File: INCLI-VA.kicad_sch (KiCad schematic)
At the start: 0 parts

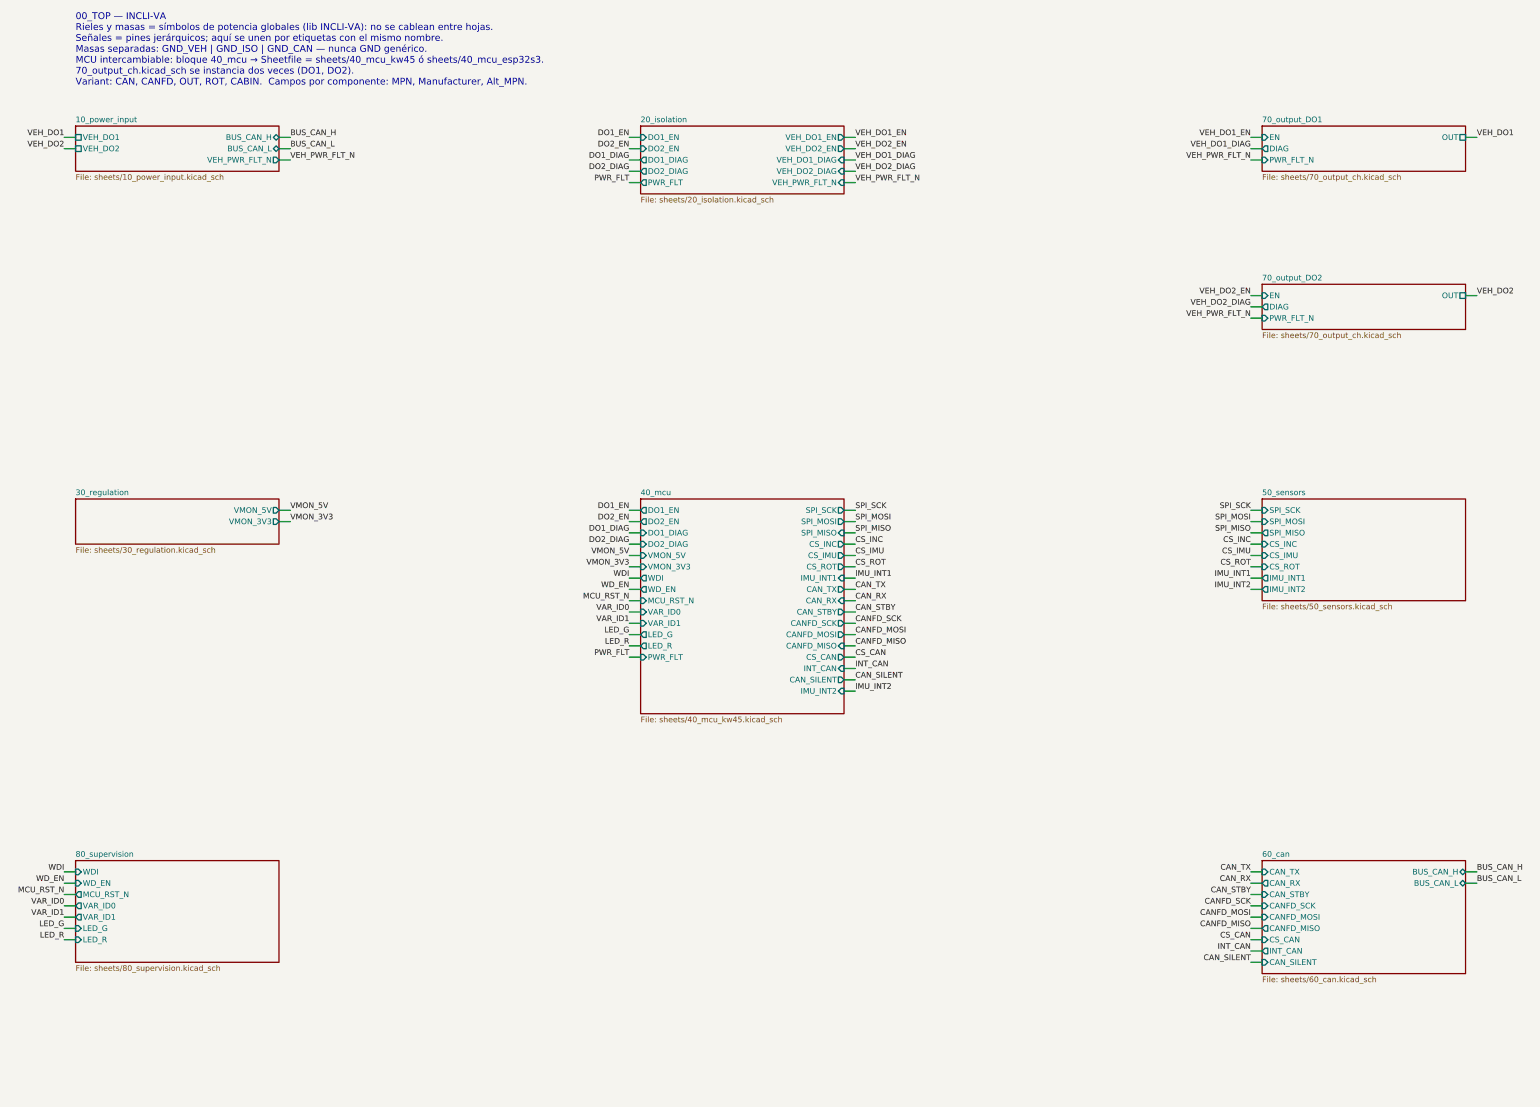
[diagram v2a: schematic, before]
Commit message: Alcance: solo ESP32-S3, CAN clásico por TWAI, sin MCP2518FD
- Raíz: el bloque 40_mcu apunta a 40_mcu_esp32s3. 40_mcu_kw45 queda en
  el repo solo como referencia, fuera de la jerarquía.
- CAN: se eliminan el MCP2518FD, el cristal y los pines CANFD_SCK/MOSI/
  MISO, CS_CAN e INT_CAN en 60_can, 40_mcu_esp32s3 y la raíz (etiquetas,
  cables y pines de hoja). TWAI nativo (J1939) directo al ADM3055E.
  Se quita la variante CANFD.
- 20_isolation (nota): PS1 >= 5 W y entrada 9-72 V (corte OV 38.4 V);
  U2 = TPS7A1650-Q1 para +5V_VEH.
- 40_mcu_esp32s3 (nota): desacople 22 uF + 100 nF según Espressif y
  límite de 47 uF en +3V3_D por el TPS62A02-Q1; solo BLE en operación.
- README: tabla corregida (LM74930-Q1 en 10_power_input, 20, 30, 40, 60),
  sección MCU y "Requisitos para el firmware" (rearme del latch >= 100 ms,
  arranque limpio tras brownout, NimBLE con WiFi desactivado).
- CLAUDE.md: sección "Alcance" (ESP32-S3 único, dimensionar con WiFi).

ERC: 180 -> 160 violaciones; sin errores nuevos. Las restantes son de
hojas sin terminar (20, 30, 60) y etiquetas de la raíz sin destino.

Co-Authored-By: Claude Opus 5.5 <noreply@anthropic.com>
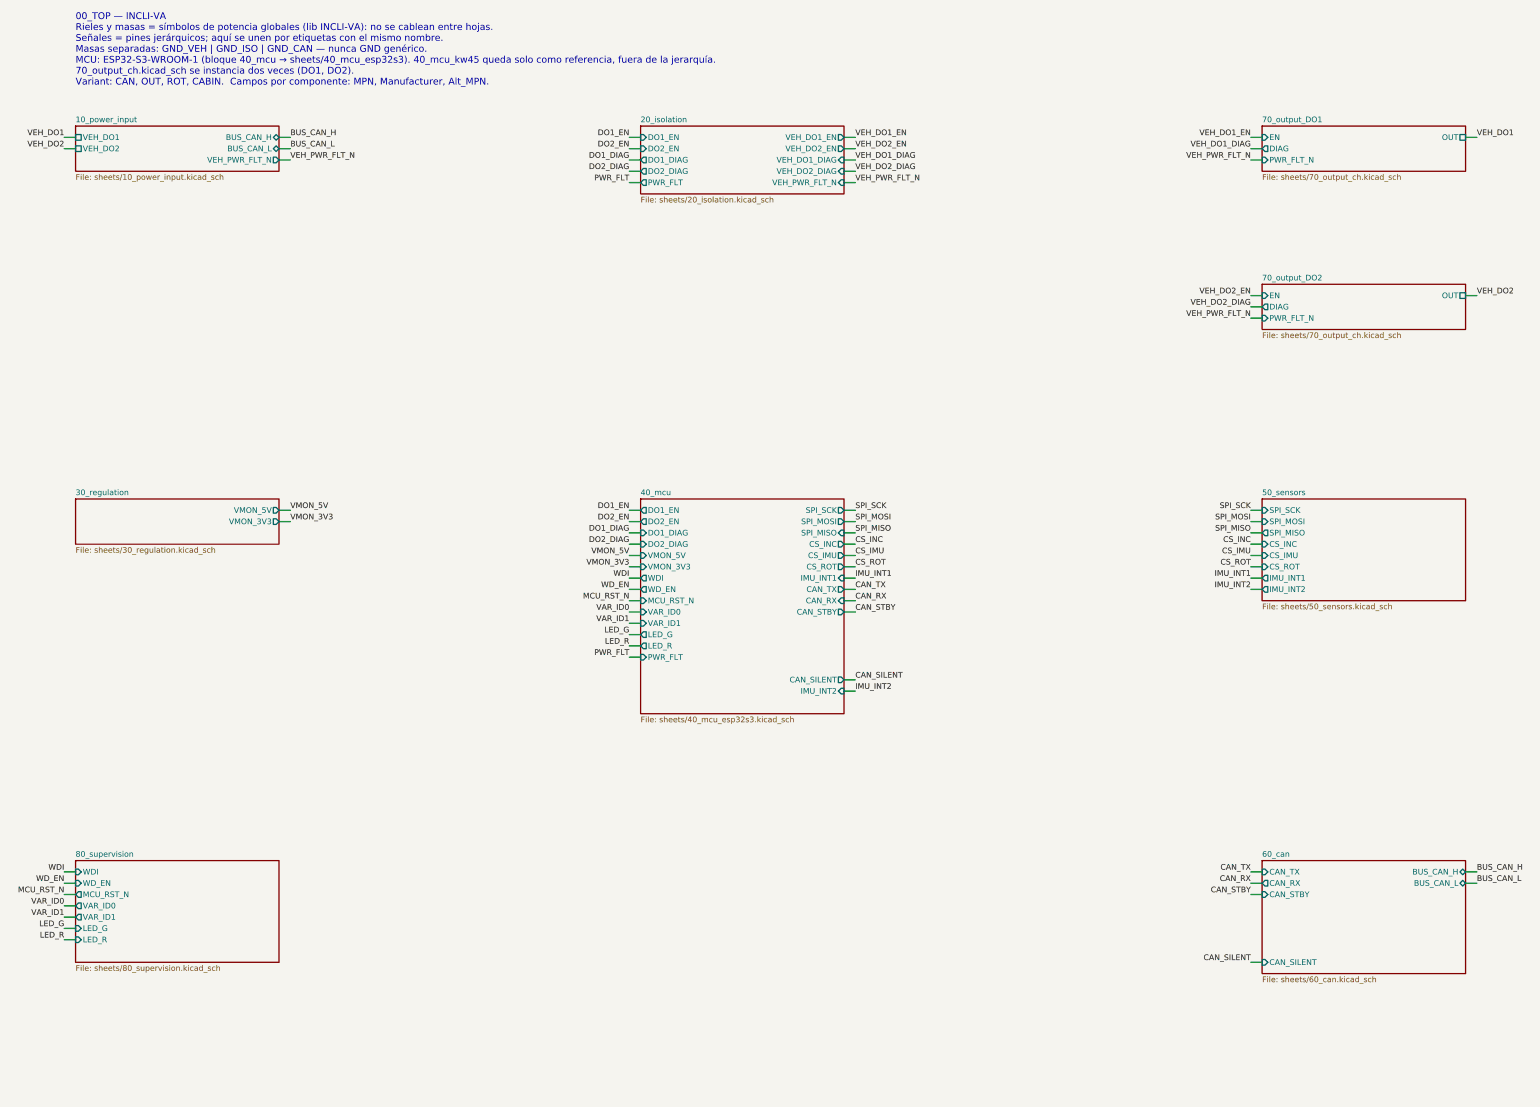
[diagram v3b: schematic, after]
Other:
- sheet 40_mcu: file sheets/40_mcu_kw45.kicad_sch -> sheets/40_mcu_esp32s3.kicad_sch
- sheet 40_mcu ports: added none; removed CANFD_MISO, CANFD_MOSI, CANFD_SCK, CS_CAN, INT_CAN
- sheet 60_can ports: added none; removed CANFD_MISO, CANFD_MOSI, CANFD_SCK, CS_CAN, INT_CAN
- note added: "00_TOP — INCLI-VA Rieles y masas = símbolos de potencia globales (lib INCLI-VA): no se cablean entre hojas. Señales = pines jerárquicos; aquí se unen por etiquetas con el mismo nombre. Masas separadas: GND_VEH | GND_ISO | GND_CAN — nunca GND genérico. MCU: ESP32-S3-WROOM-1 (bloque 40_mcu → sheets/40_mcu_esp32s3). 40_mcu_kw45 queda solo como referencia, fuera de la jerarquía. 70_output_ch.kicad_sc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"
- note removed: "00_TOP — INCLI-VA Rieles y masas = símbolos de potencia globales (lib INCLI-VA): no se cablean entre hojas. Señales = pines jerárquicos; aquí se unen por etiquetas con el mismo nombre. Masas separadas: GND_VEH | GND_ISO | GND_CAN — nunca GND genérico. MCU intercambiable: bloque 40_mcu → Sheetfile = sheets/40_mcu_kw45 ó sheets/40_mcu_esp32s3. 70_output_ch.kicad_sch se instancia dos veces (DO1, DO2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"

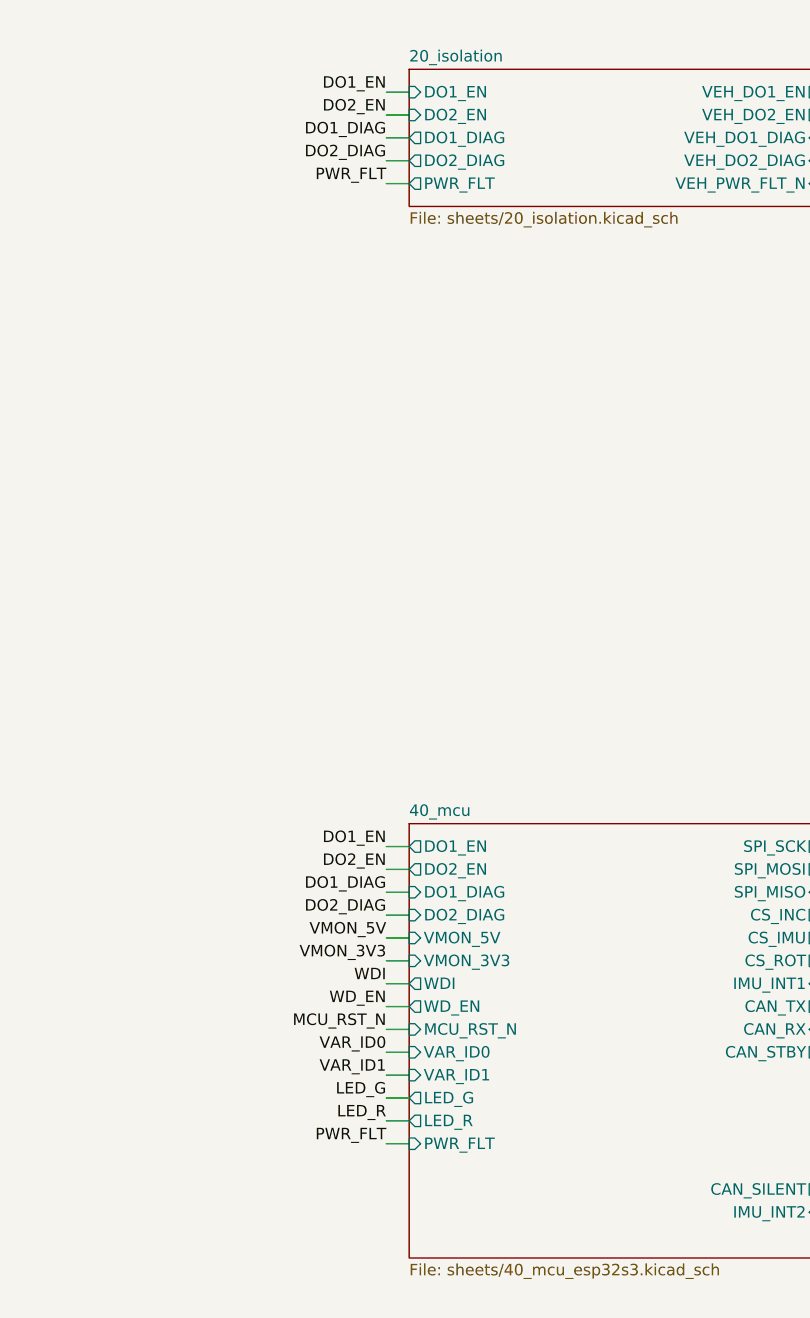
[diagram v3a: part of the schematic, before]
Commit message: 20_isolation: PS201 EC4AW8-48S05, LDO +5V_VEH, ISO7763-Q1; PWR_FLT_N; L301 HandSolder
- Hoja 20 completa: PS201 Cincon EC4AW8-48S05 (sin Remote On/Off) con
  C201/C202/C203; U201 TPS7A1650-Q1 (+VPROT -> +5V_VEH; DELAY, PG y FB/NC
  abiertos según TI SBVS188E tabla 5-1); U202 ISO7763FQDWRQ1 con pull-downs
  R201-R204; notas de distancias de la barrera 1.
- Símbolo INCLI-VA:EC4AW8-48S05 creado desde la tabla de pines del datasheet
  Cincon V10 (excepción autorizada); huella oficial TRACO THD 15WIN verificada.
- Renombre PWR_FLT -> PWR_FLT_N en la raíz, 20 y 40_mcu.
- Huella INCLI-VA:L_Coilcraft_XAL4020_HandSolder (Coilcraft Doc 806-4,
  rev. 02/25/26) asignada a L301.
- Datasheets de EC4AW8 y XAL4020 en docs/datasheets.
- ERC: 0 en 20 y 30 (129 en el proyecto); sch_visual_qa PASS en 20.

Co-Authored-By: Claude Opus 5.5 <noreply@anthropic.com>
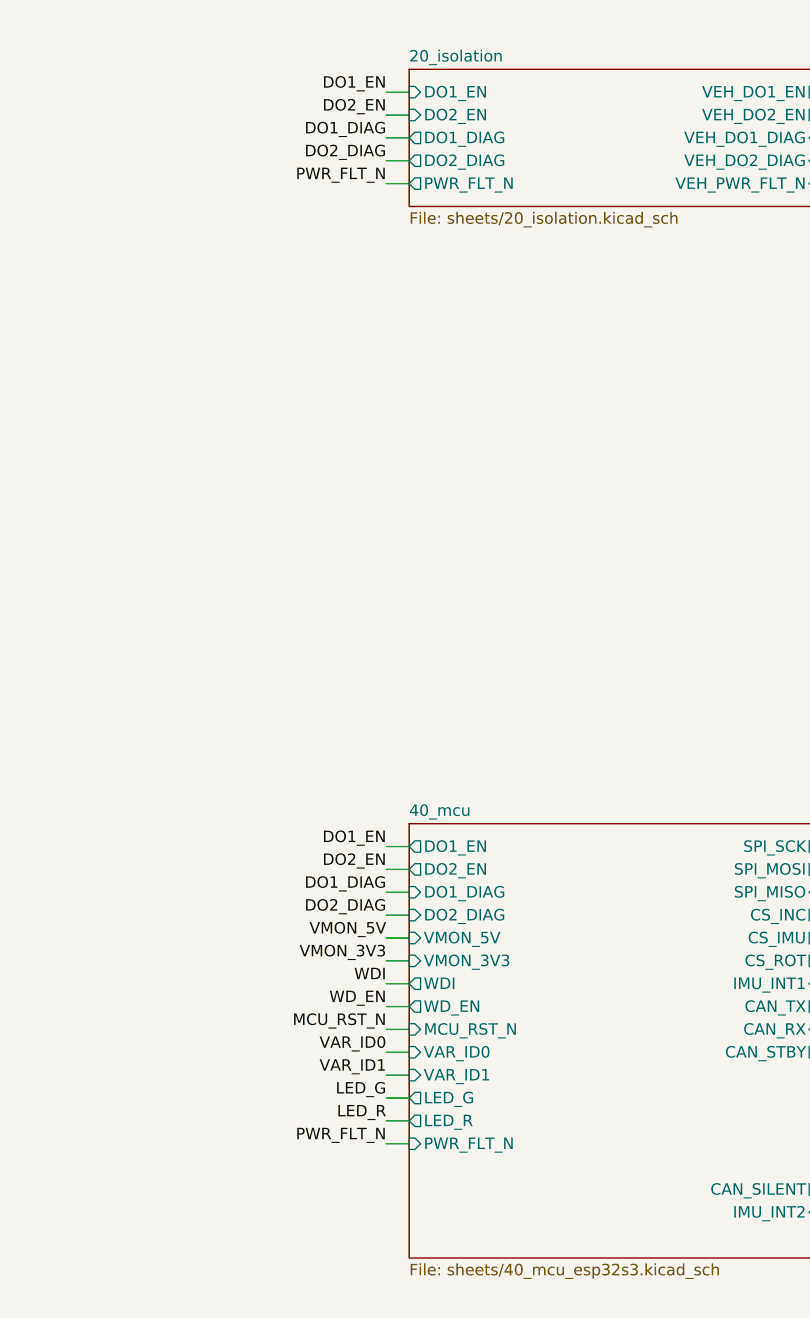
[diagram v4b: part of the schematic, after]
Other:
- sheet 20_isolation ports: added PWR_FLT_N; removed PWR_FLT
- sheet 40_mcu ports: added PWR_FLT_N; removed PWR_FLT
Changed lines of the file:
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@@
 		)
 	)
-	(label "PWR_FLT"
+	(label "PWR_FLT_N"
 		(at 154.94 160.02 180)
 		(effects
@@
 		)
 	)
-	(label "PWR_FLT"
+	(label "PWR_FLT_N"
 		(at 154.94 53.34 180)
 		(effects
@@
 			)
 		)
-		(pin "PWR_FLT" output
+		(pin "PWR_FLT_N" output
 			(at 157.48 53.34 180)
 			(effects
@@
 			)
 		)
-		(pin "PWR_FLT" input
+		(pin "PWR_FLT_N" input
 			(at 157.48 160.02 180)
 			(effects

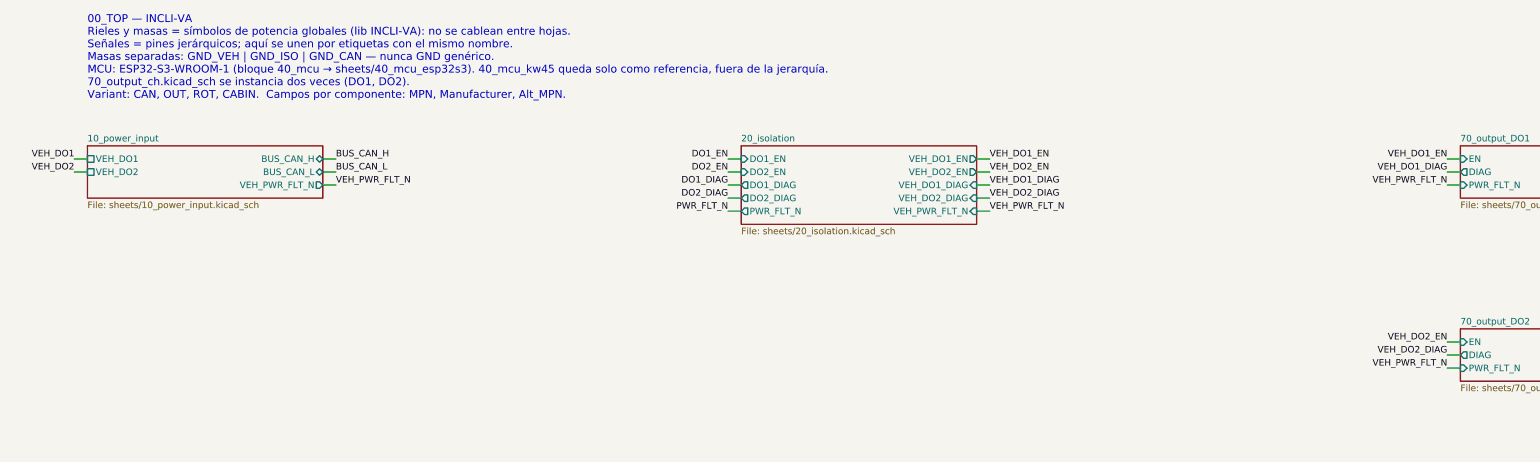
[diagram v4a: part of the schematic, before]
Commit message: [Claude Code] 20_buck_5v: opción B (no aislada) con LMR38010; masas unificadas
- sheets/20_isolation -> sheets/20_buck_5v: se quitan PS201, ISO7763 y
  TPS7A1650; U201 LMR38010SQDDARQ1 (PROTO: LMR38010SDDAR, LCSC C5219310),
  5.02 V / 1 A a 400 kHz según TI SNVSC73B (L201 XAL6060-333, 3 x 22 uF,
  RT 64.9k, FB 100k/24.9k). Huella oficial HSOIC-8 con vías térmicas.
- Símbolo LMR38010 (easyeda2kicad) en lib/easyeda2kicad/INCLI-VA_easyeda,
  con tipos de pin ajustados; registrado en sym-lib-table.
- Todas las hojas: GND_ISO -> GND_VEH, +5V_ISO -> +5V_VEH.
- Raíz: EN/DIAG/FLT directos entre las hojas 40, 70 y 10; la hoja 20 sin pines.
- 10_power_input: R111 a +3V3_D, C109 = 100 nF (inrush con C105),
  C105 DNP solo en PROTO; se quita un PWR_FLAG suelto en GND_VEH.
- 70_output_ch: cambios de layout del usuario (hechos en KiCad).
- Textos de las hojas 30/40/50/80 y la raíz sin referencias al aislamiento.
- ERC: 0 en 10, 20, 30, 40, 50, 60 y 70; quedan los de 80 (hoja vacía).

Co-Authored-By: Claude Opus 5.5 <noreply@anthropic.com>
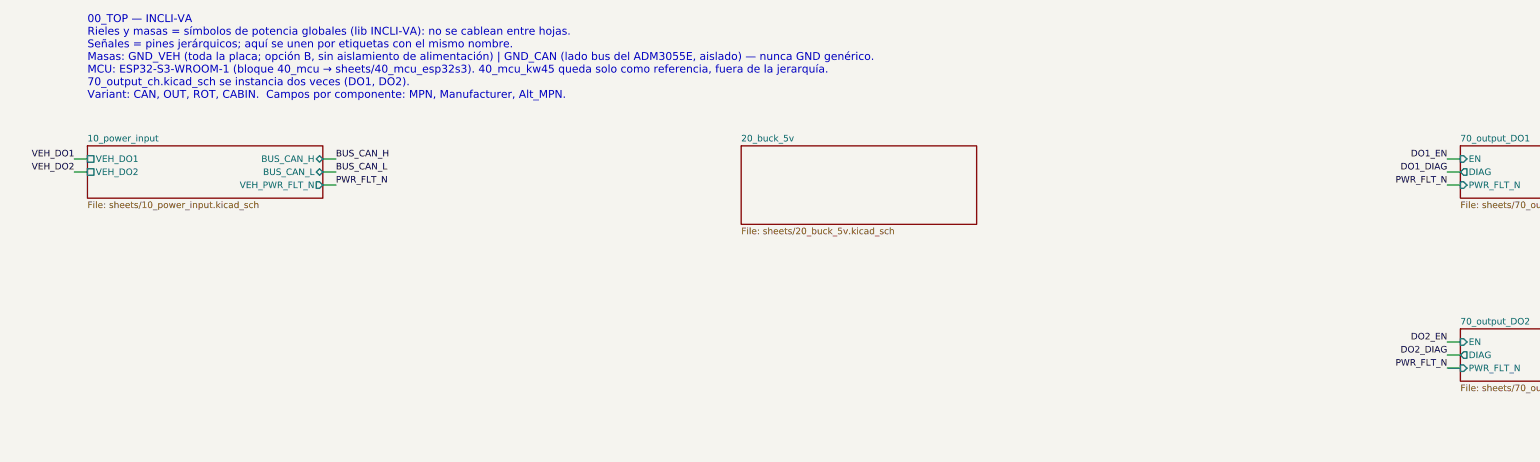
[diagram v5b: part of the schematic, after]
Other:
- sheet 20_isolation renamed 20_buck_5v
- sheet 20_buck_5v: file sheets/20_isolation.kicad_sch -> sheets/20_buck_5v.kicad_sch
- sheet 20_buck_5v ports: added none; removed DO1_DIAG, DO1_EN, DO2_DIAG, DO2_EN, PWR_FLT_N, VEH_DO1_DIAG, VEH_DO1_EN, VEH_DO2_DIAG, VEH_DO2_EN, VEH_PWR_FLT_N
- note added: "00_TOP — INCLI-VA Rieles y masas = símbolos de potencia globales (lib INCLI-VA): no se cablean entre hojas. Señales = pines jerárquicos; aquí se unen por etiquetas con el mismo nombre. Masas: GND_VEH (toda la placa; opción B, sin aislamiento de alimentación) | GND_CAN (lado bus del ADM3055E, aislado) — nunca GND genérico. MCU: ESP32-S3-WROOM-1 (bloque 40_mcu → sheets/40_mcu_esp32s3). 40_mcu_kw45 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"
- note removed: "00_TOP — INCLI-VA Rieles y masas = símbolos de potencia globales (lib INCLI-VA): no se cablean entre hojas. Señales = pines jerárquicos; aquí se unen por etiquetas con el mismo nombre. Masas separadas: GND_VEH | GND_ISO | GND_CAN — nunca GND genérico. MCU: ESP32-S3-WROOM-1 (bloque 40_mcu → sheets/40_mcu_esp32s3). 40_mcu_kw45 queda solo como referencia, fuera de la jerarquía. 70_output_ch.kicad_sc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"
